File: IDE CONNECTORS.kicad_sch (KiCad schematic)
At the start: 33 parts, among them J14 PRIMARY IDE CONN., J15 SECONDARY IDE CONN.

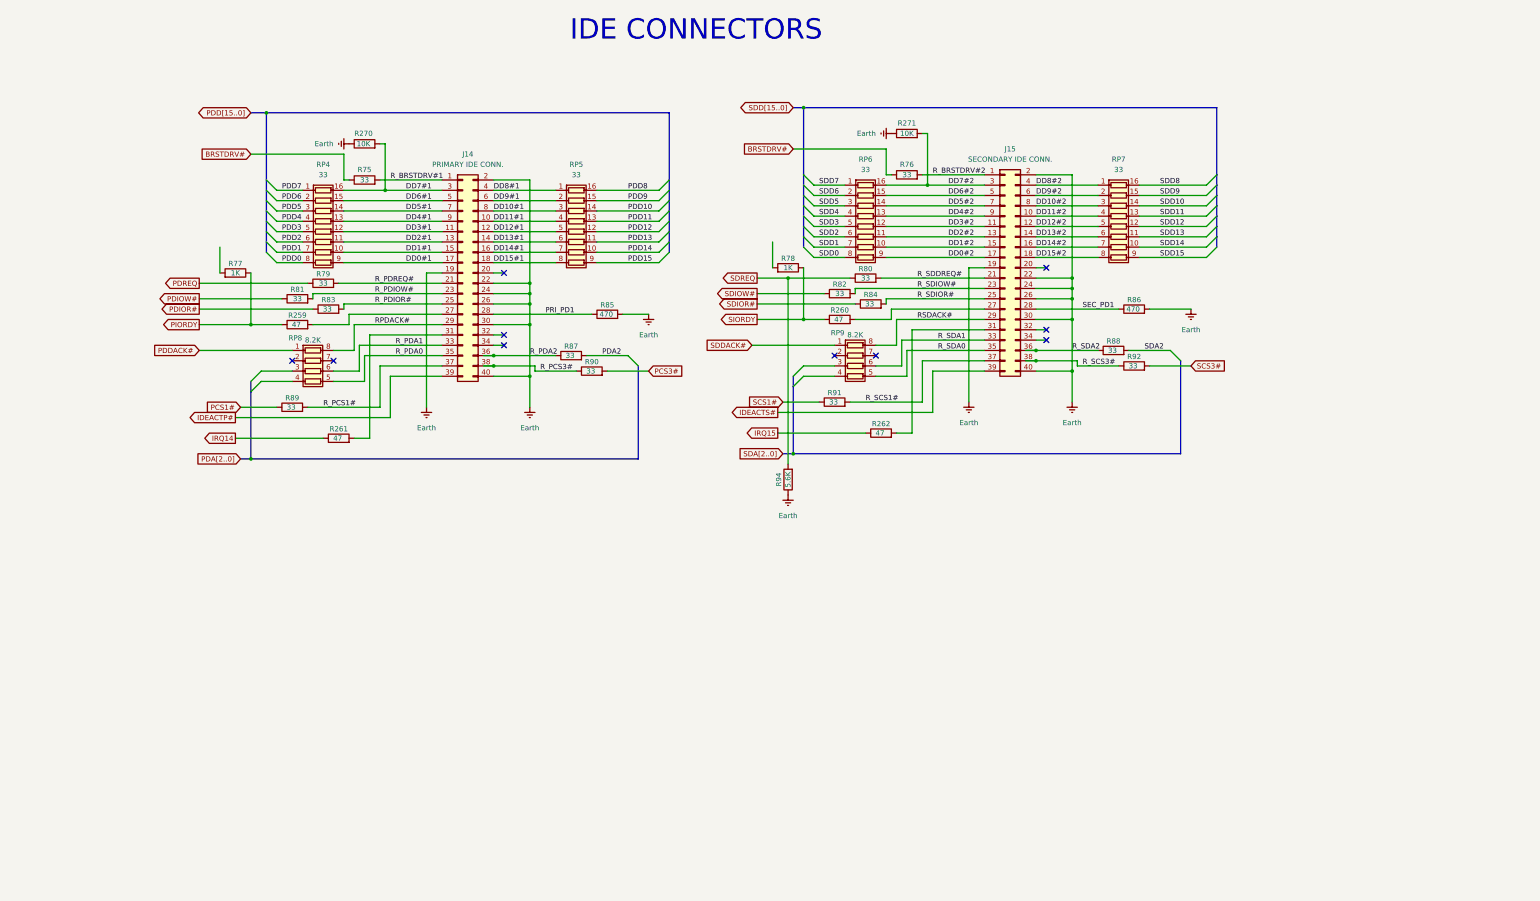
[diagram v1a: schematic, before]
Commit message: page 19 IDE connectors
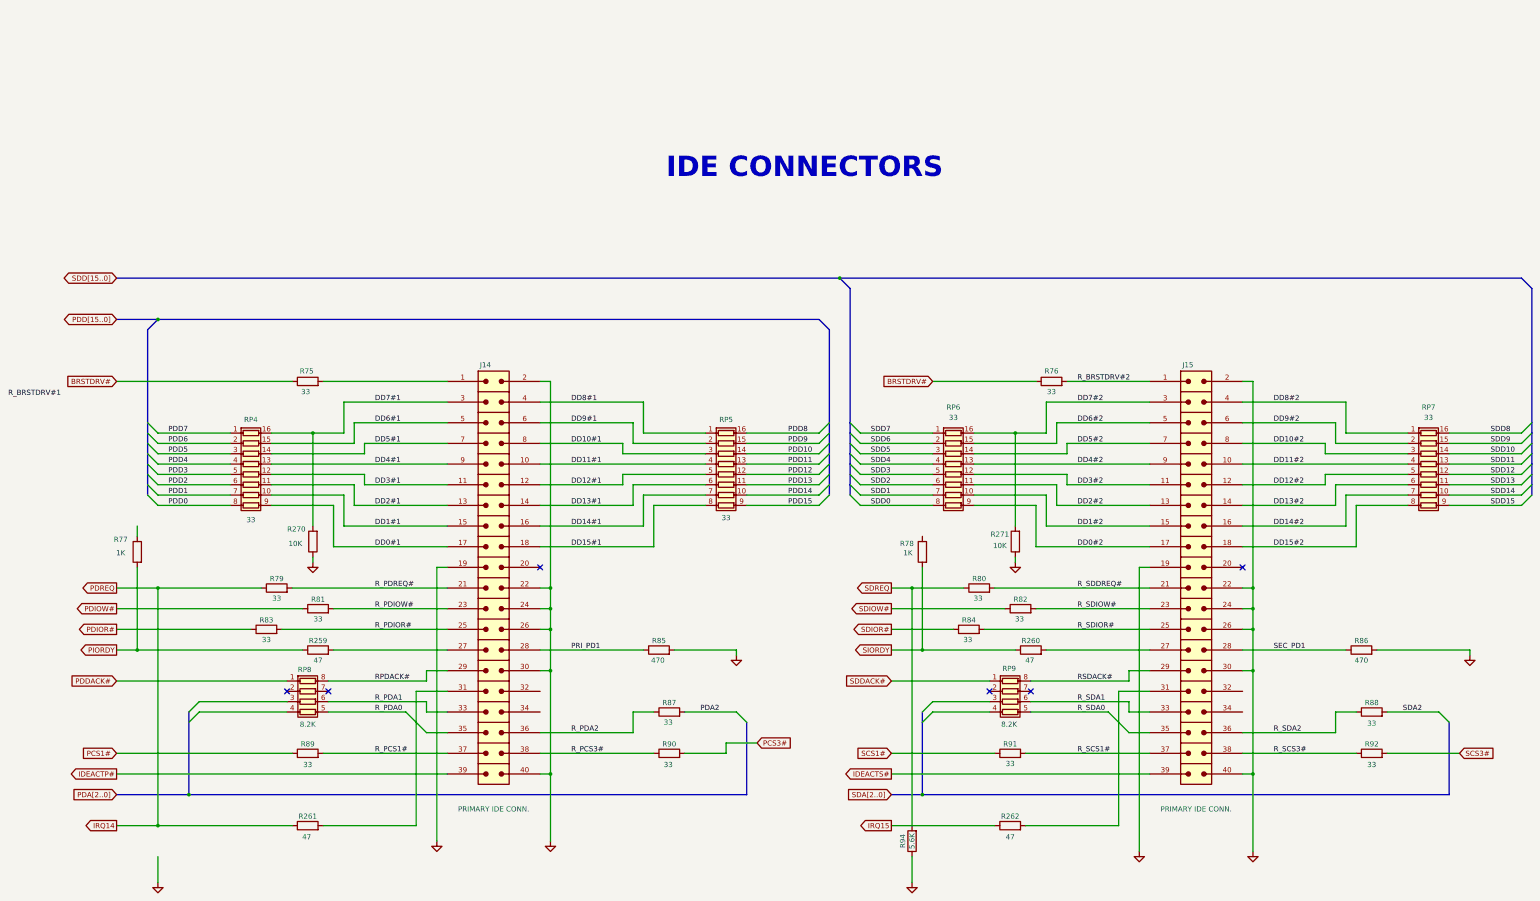
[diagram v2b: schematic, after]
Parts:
- removed J14: PRIMARY IDE CONN., Connector_IDC:IDC-Header_2x20_P2.54mm_Vertical, symbol Connector_Generic:Conn_02x20_Odd_Even
- removed J15: SECONDARY IDE CONN., Connector_IDC:IDC-Header_2x20_P2.54mm_Vertical, symbol Connector_Generic:Conn_02x20_Odd_Even
- added J14, J15: PRIMARY IDE CONN., Connector_IDC:IDC-Header_2x20_P2.54mm_Vertical, symbol P2-3_era:IDE_Connector
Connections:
- net PDREQ is gone; now on net IRQ14: R79.1
- net DD0#1: now also J14.17
- net DD0#2: now also J15.17
- net DD1#1: now also J14.15
- net DD1#2: now also J15.15
- net DD10#1: now also J14.8
- net DD10#2: now also J15.8
- net DD11#1: now also J14.10
- net DD11#2: now also J15.10
- net DD12#1: now also J14.12
- net DD12#2: now also J15.12
- net DD13#1: now also J14.14
- net DD13#2: now also J15.14
- net DD14#1: now also J14.16
- net DD14#2: now also J15.16
- net DD15#1: now also J14.18
- net DD15#2: now also J15.18
- net DD2#1: now also J14.13
- net DD2#2: now also J15.13
- net DD3#1: now also J14.11
- net DD3#2: now also J15.11
- net DD4#1: now also J14.9
- net DD4#2: now also J15.9
- net DD5#1: now also J14.7
- net DD5#2: now also J15.7
- net DD6#1: now also J14.5
- net DD6#2: now also J15.5
- net DD7#1: now also J14.3
- net DD7#2: now also J15.3
- net DD8#1: now also J14.4
- net DD8#2: now also J15.4
- net DD9#1: now also J14.6
- net DD9#2: now also J15.6
- net IDEACTP#: now also J14.39
- net IDEACTS#: now also J15.39
- net PIORDY: now also R77.2; no longer R77.1
- net PRI_PD1: now also J14.28
- net RPDACK#: now also J14.29
- net RSDACK#: now also J15.29
- net R_BRSTDRV#1: no longer R75.2
- net R_BRSTDRV#2: now also J15.1
- net R_PCS1#: now also J14.37
- net R_PCS3#: now also J14.38
- net R_PDA0: now also J14.35
- net R_PDA1: now also J14.33
- net R_PDIOR#: now also J14.25
- net R_PDIOW#: now also J14.23
- net R_PDREQ#: now also J14.21
- net R_SCS1#: now also J15.37
- net R_SCS3#: now also J15.38
- net R_SDA0: now also J15.35
- net R_SDA1: now also J15.33
- net R_SDDREQ#: now also J15.21
- net R_SDIOR#: now also J15.25
- net R_SDIOW#: now also J15.23
- net SEC_PD1: now also J15.28
- net SIORDY: now also R78.2; no longer R78.1
- net at R259.2: now also J14.27
- net at R261.2: now also J14.31
- net at R260.2: now also J15.27
- net at R262.2: now also J15.31
- net Earth renamed GND
- net GND: now also J14.19, J14.2, J14.22, J14.24, J14.26, J14.30, J14.40, J15.19, J15.2, J15.22, J15.24, J15.26, J15.30, J15.40; no longer R87.1, R88.1
- new net: J14.1, R75.2
- new net R_PDA2: J14.36, R87.1
- new net R_SDA2: J15.36, R88.1
- no-connect marks 10 -> 6
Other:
- title: (none) -> PCI IDE CONNECTORS
- moved on the sheet: R259, R260, R261, R262, R270, R271, R75, R76, R77, R78, R79, R80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

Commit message: page 6,7,8 82443BX chipset, various small fixes
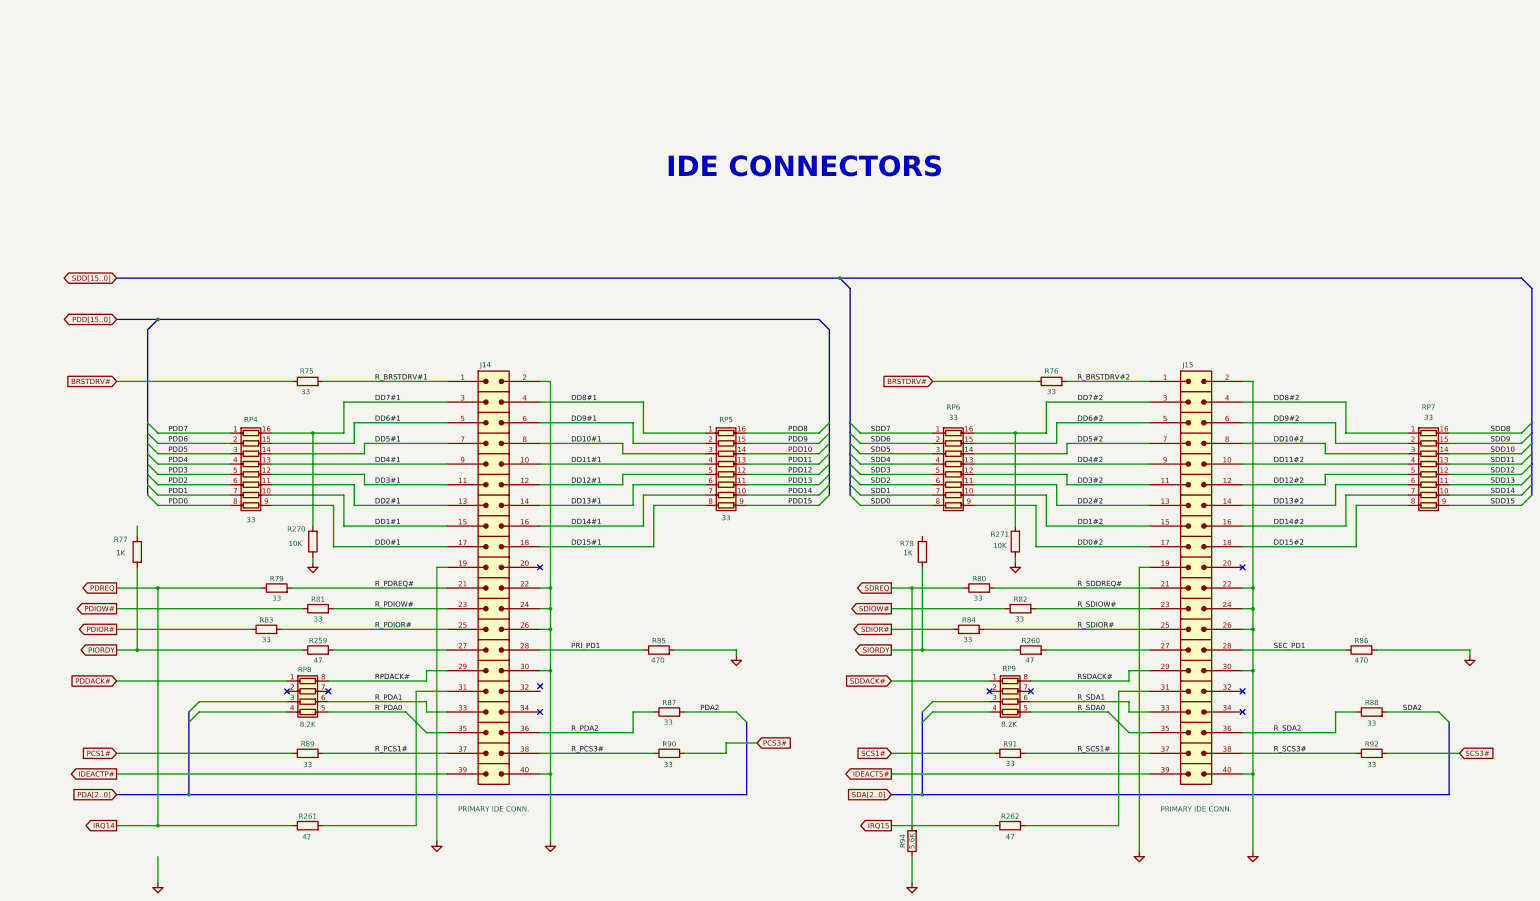
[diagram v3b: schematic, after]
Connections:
- net R_BRSTDRV#1: now also J14.1, R75.2
- no-connect marks 6 -> 10
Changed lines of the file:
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@@
 	)
 	(no_connect
+		(at 154.94 193.04)
+	)
+	(no_connect
 		(at 327.66 157.48)
 	)
@@
 	)
 	(no_connect
+		(at 154.94 186.69)
+	)
+	(no_connect
 		(at 154.94 157.48)
 	)
@@
 	)
 	(no_connect
+		(at 327.66 187.96)
+	)
+	(no_connect
 		(at 102.87 187.96)
 	)
@@
 		(at 275.59 187.96)
 	)
+	(no_connect
+		(at 327.66 193.04)
+	)
 	(bus_entry
 		(at 58.42 132.08)
@@
 	)
 	(label "R_BRSTDRV#1"
-		(at 24.13 115.57 0)
+		(at 114.3 111.76 0)
 		(fields_autoplaced yes)
 		(effects
@@
 			)
 		)
-		(property "Datasheet" "~"
+		(property "Datasheet" ""
 			(at 142.24 160.02 0)
 			(effects
@@
 			)
 		)
-		(property "Datasheet" "~"
+		(property "Datasheet" ""
 			(at 314.96 160.02 0)
 			(effects
